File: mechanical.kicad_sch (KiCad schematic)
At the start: 8 parts

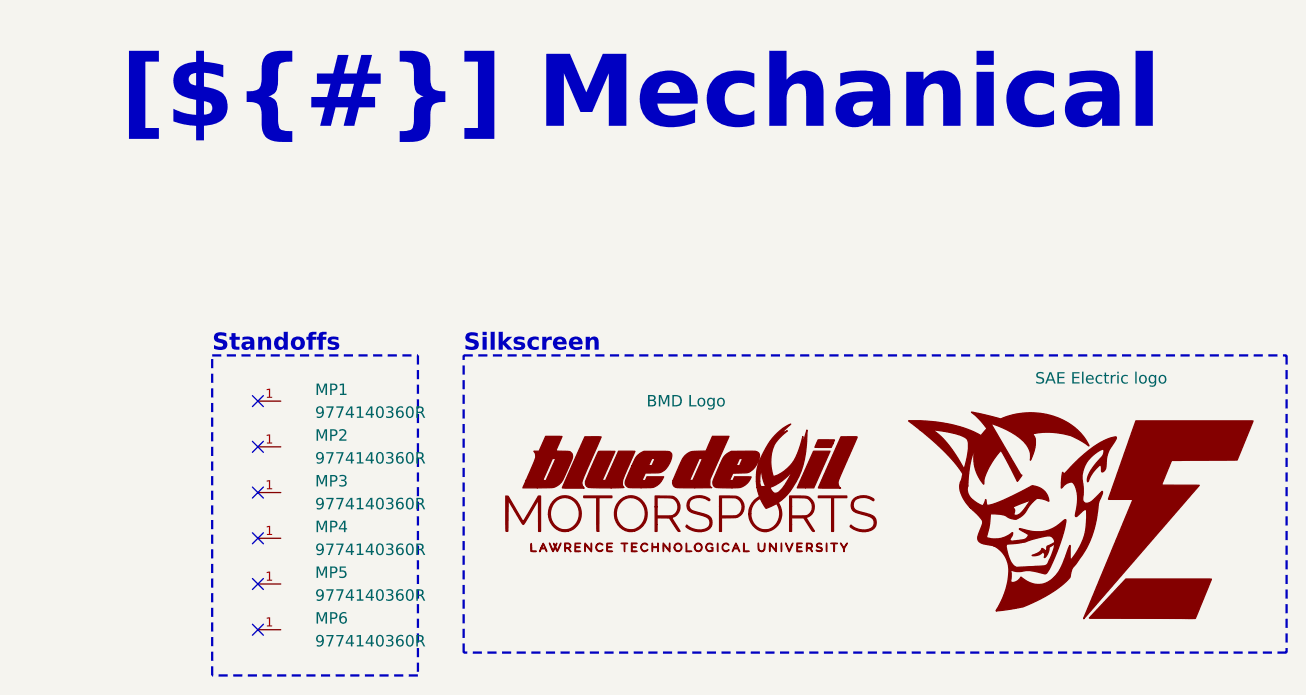
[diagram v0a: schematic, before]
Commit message: PCB[Routing, Mechanical, Silk]: Inital routing, Finalized mounting points and board to board connector reltive posision, and inital silkscreen. SCH[Labels]: Updated labels to match BMS_Slave board.
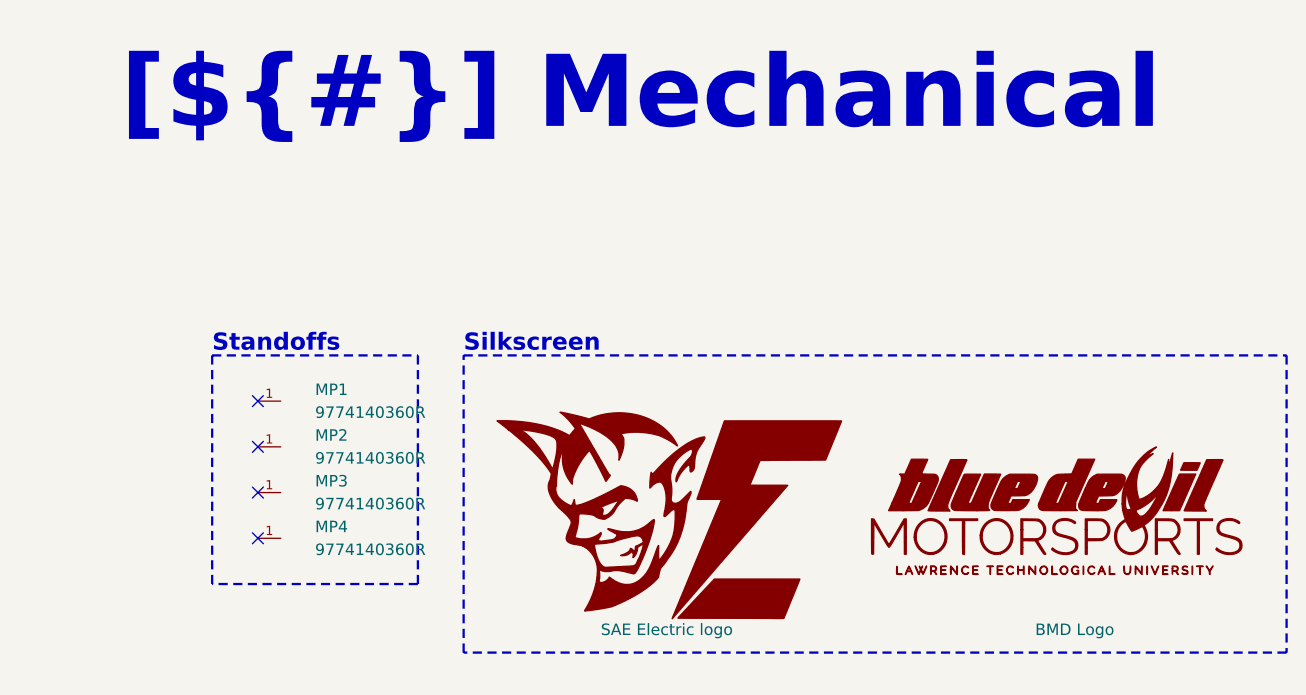
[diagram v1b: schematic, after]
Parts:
- removed MP5, MP6: 9774140360R, remote_9774140360r:WA-SMSI_9774140360, symbol remote_9774140360r:WA-SMSI_9774XXX360
- G1: footprint remote_bmd_logo:BDM_Logo_20mm -> remote_bmd_logo:BDM_Logo_40mm
- G2: footprint remote_sae_electric_logo:SAE_Electric_Logo_10mm -> remote_sae_electric_logo:SAE_Electric_Logo_20mm
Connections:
- no-connect marks 6 -> 4
